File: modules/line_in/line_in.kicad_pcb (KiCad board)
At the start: 2 copper layers, 27.9 x 66 mm, 2 parts

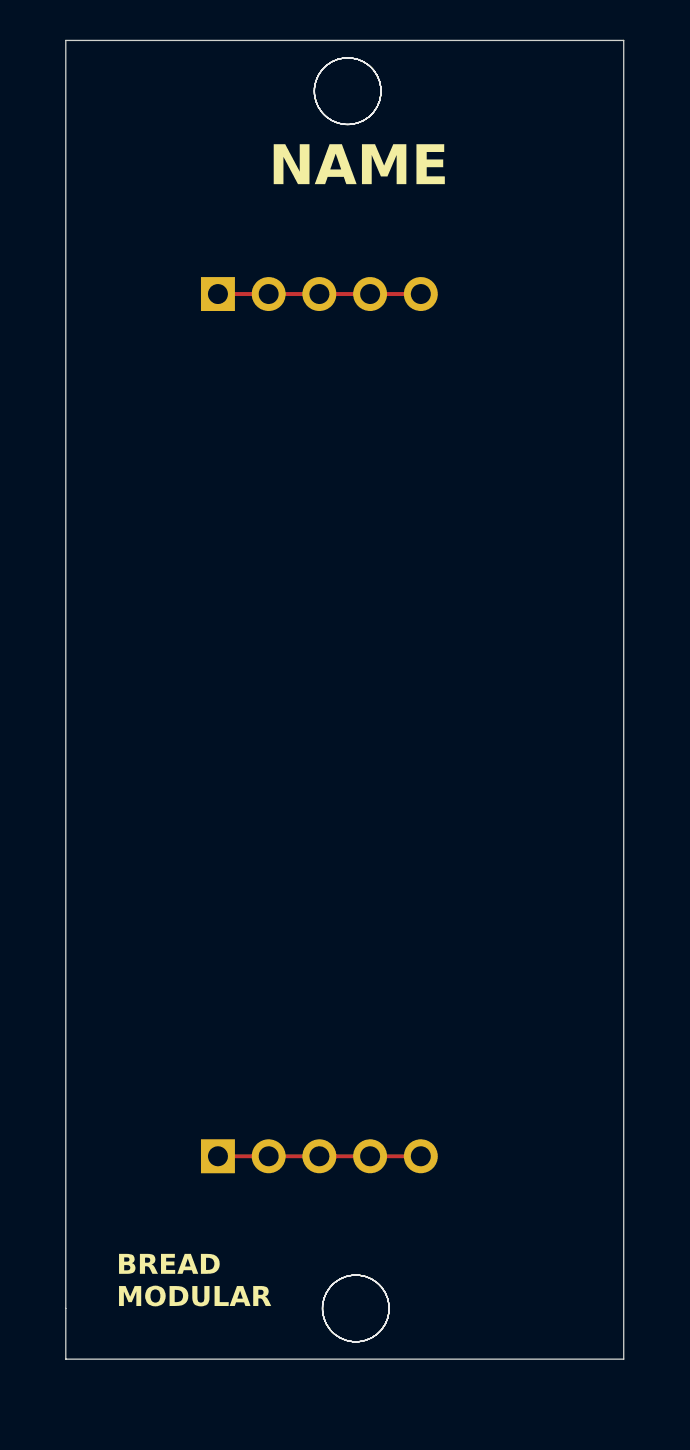
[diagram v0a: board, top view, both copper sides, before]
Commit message: Add the schematic for the PCB
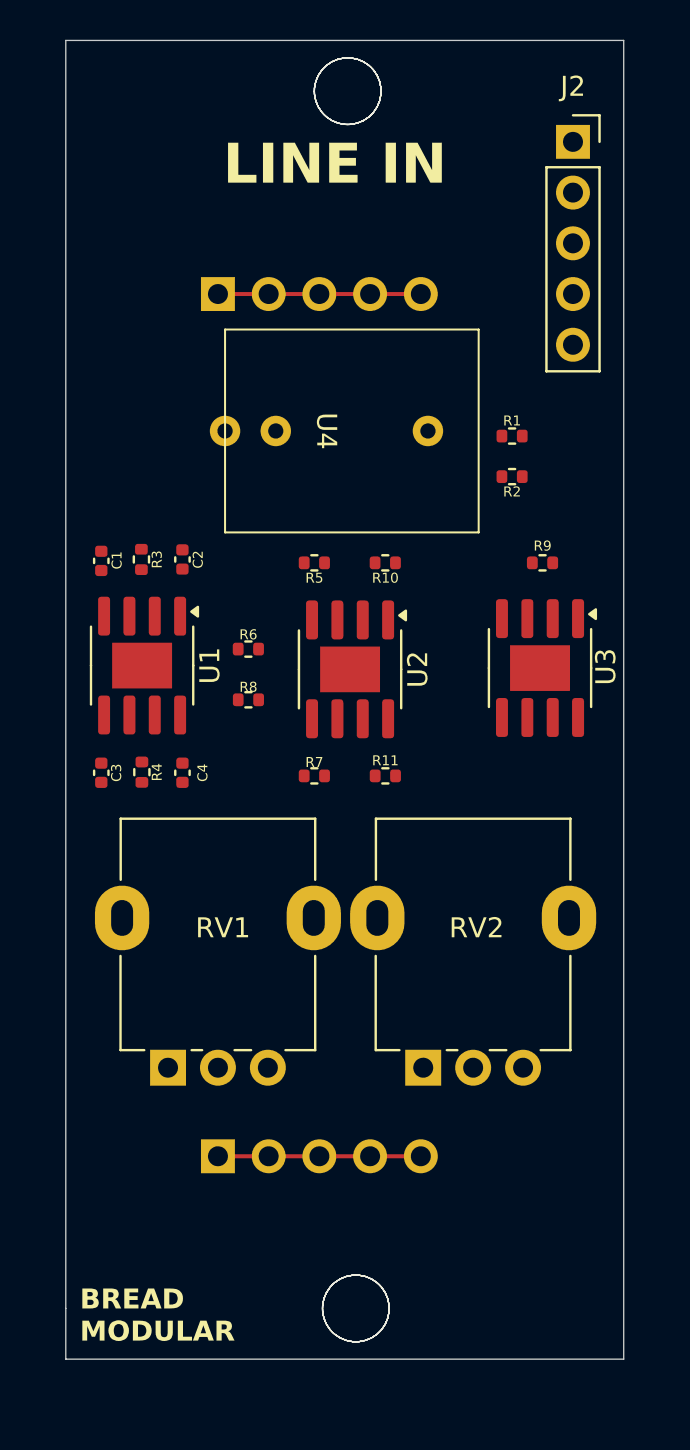
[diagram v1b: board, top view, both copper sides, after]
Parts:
- added C1: 0.1uf, Capacitor_SMD:C_0402_1005Metric, F.Cu at (50.0, 66.7)
- added C2: 33pf, Capacitor_SMD:C_0402_1005Metric, F.Cu at (54.1, 66.6)
- added C3: 0.1uf, Capacitor_SMD:C_0402_1005Metric, F.Cu at (50.0, 77.3)
- added C4: 33pf, Capacitor_SMD:C_0402_1005Metric, F.Cu at (54.1, 77.3)
- added J2: Outputs, Connector_PinSocket_2.54mm:PinSocket_1x05_P2.54mm_Vertical, F.Cu at (73.7, 45.7)
- added R1: 1K, Resistor_SMD:R_0402_1005Metric, F.Cu at (70.6, 60.5)
- added R10: 100K, Resistor_SMD:R_0402_1005Metric, F.Cu at (64.3, 66.8)
- added R11: 100K, Resistor_SMD:R_0402_1005Metric, F.Cu at (64.3, 77.5)
- added R2: 1K, Resistor_SMD:R_0402_1005Metric, F.Cu at (70.6, 62.5)
- added R3: 100K, Resistor_SMD:R_0402_1005Metric, F.Cu at (52.0, 66.6)
- added R4: 100K, Resistor_SMD:R_0402_1005Metric, F.Cu at (52.1, 77.3)
- added R5: 100K, Resistor_SMD:R_0402_1005Metric, F.Cu at (60.7, 66.8)
- added R6: 10K, Resistor_SMD:R_0402_1005Metric, F.Cu at (57.4, 71.1)
- added R7: 100K, Resistor_SMD:R_0402_1005Metric, F.Cu at (60.7, 77.5)
- added R8: 10K, Resistor_SMD:R_0402_1005Metric, F.Cu at (57.4, 73.7)
- added R9: 51K, Resistor_SMD:R_0402_1005Metric, F.Cu at (72.1, 66.8)
- added RV1: 100K, Potentiometer_THT:Potentiometer_Alpha_RD901F-40-00D_Single_Vertical, F.Cu at (53.4, 92.1)
- added RV2: 100K, Potentiometer_THT:Potentiometer_Alpha_RD901F-40-00D_Single_Vertical, F.Cu at (66.2, 92.1)
- added U1: LM358, Package_SO:SOIC-8-1EP_3.9x4.9mm_P1.27mm_EP2.29x3mm, F.Cu at (52.1, 71.9)
- added U2: LM358, Package_SO:SOIC-8-1EP_3.9x4.9mm_P1.27mm_EP2.29x3mm, F.Cu at (62.5, 72.1)
- added U3: LM358, Package_SO:SOIC-8-1EP_3.9x4.9mm_P1.27mm_EP2.29x3mm, F.Cu at (72.0, 72.1)
- added U4: ~, Footprints:Audio_Socket_TRS_3.5mm, F.Cu at (61.3, 60.2)
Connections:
- 5V1 pad 1: unconnected-(5V1-Pin_1-Pad1) -> +5V
- 5V1 pad 2: unconnected-(5V1-Pin_2-Pad2) -> +5V
- 5V1 pad 3: unconnected-(5V1-Pin_3-Pad3) -> +5V
- 5V1 pad 4: unconnected-(5V1-Pin_4-Pad4) -> +5V
- 5V1 pad 5: unconnected-(5V1-Pin_5-Pad5) -> +5V
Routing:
- net Net-(U1A-+): track 0.00 -> 0.71 mm
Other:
- board text added: "LINE IN"
- board text removed: "NAME"

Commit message: Update the line-in module
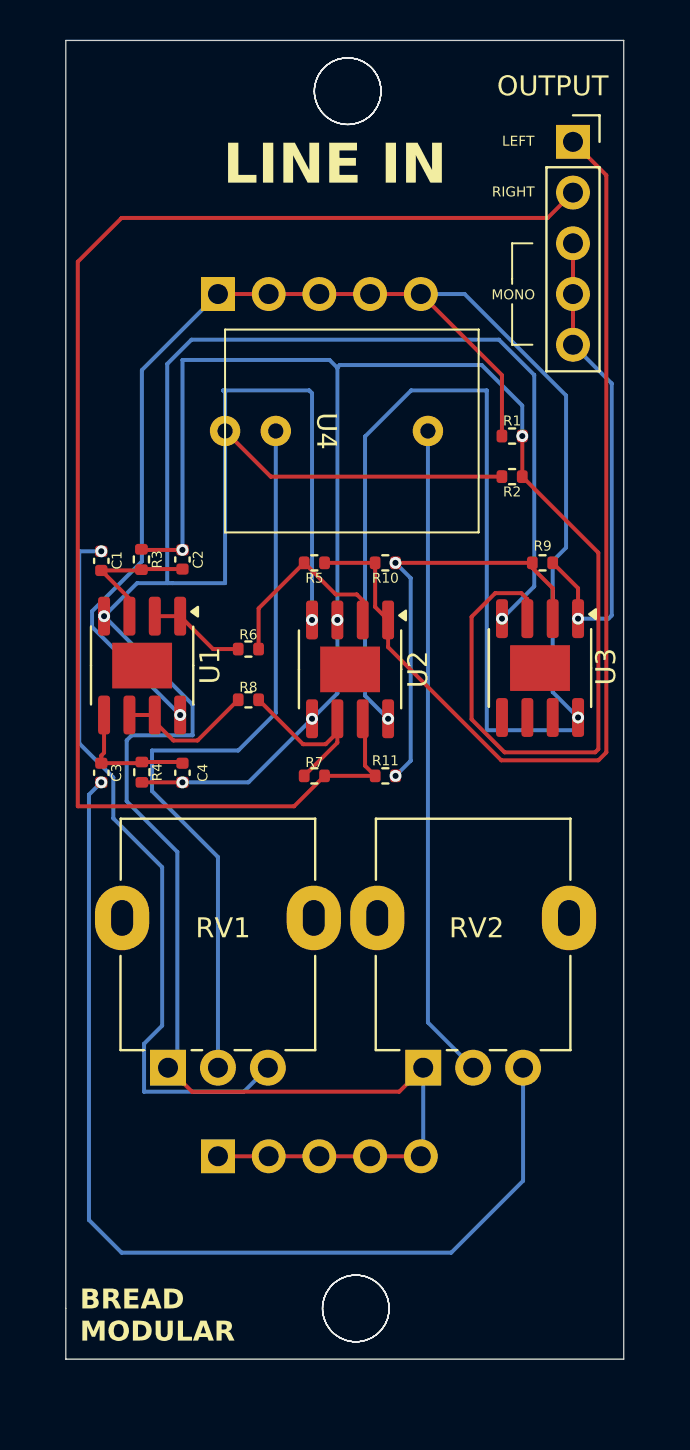
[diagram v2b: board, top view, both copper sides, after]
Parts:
- renumbered J2 to OUTPUT
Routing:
- net GND: track 10.2 -> 147.9 mm, vias 0 -> 3
- net +5V: track 0.00 -> 104.5 mm, vias 0 -> 3
- net Net-(U2A-+): track 0.00 -> 93.0 mm, vias 0 -> 5
- net OUT_R: track 0.00 -> 72.1 mm
- net IN R: track 0.00 -> 51.7 mm, vias 0 -> 1
- net OUT_L: track 0.00 -> 51.7 mm
- net Net-(U4-TIP): track 0.00 -> 38.4 mm
- net IN L: track 0.00 -> 37.0 mm, vias 0 -> 1
- net Net-(U4-RING): track 0.00 -> 32.8 mm
- net OUT_MONO: track 0.00 -> 24.5 mm, vias 0 -> 1
- net Net-(U3A--): track 0.00 -> 21.4 mm, vias 0 -> 2
- net Net-(U2A--): track 0.00 -> 9.95 mm
- net Net-(U2B--): track 0.00 -> 9.35 mm
- net Net-(U1B--): track 0.00 -> 7.02 mm
- net Net-(U1B-+): track 0.00 -> 6.58 mm
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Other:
- board text added: "LEFT"
- board text added: "MONO"
- board text added: "RIGHT"

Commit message: Make sure SMD via are not placed on pads.
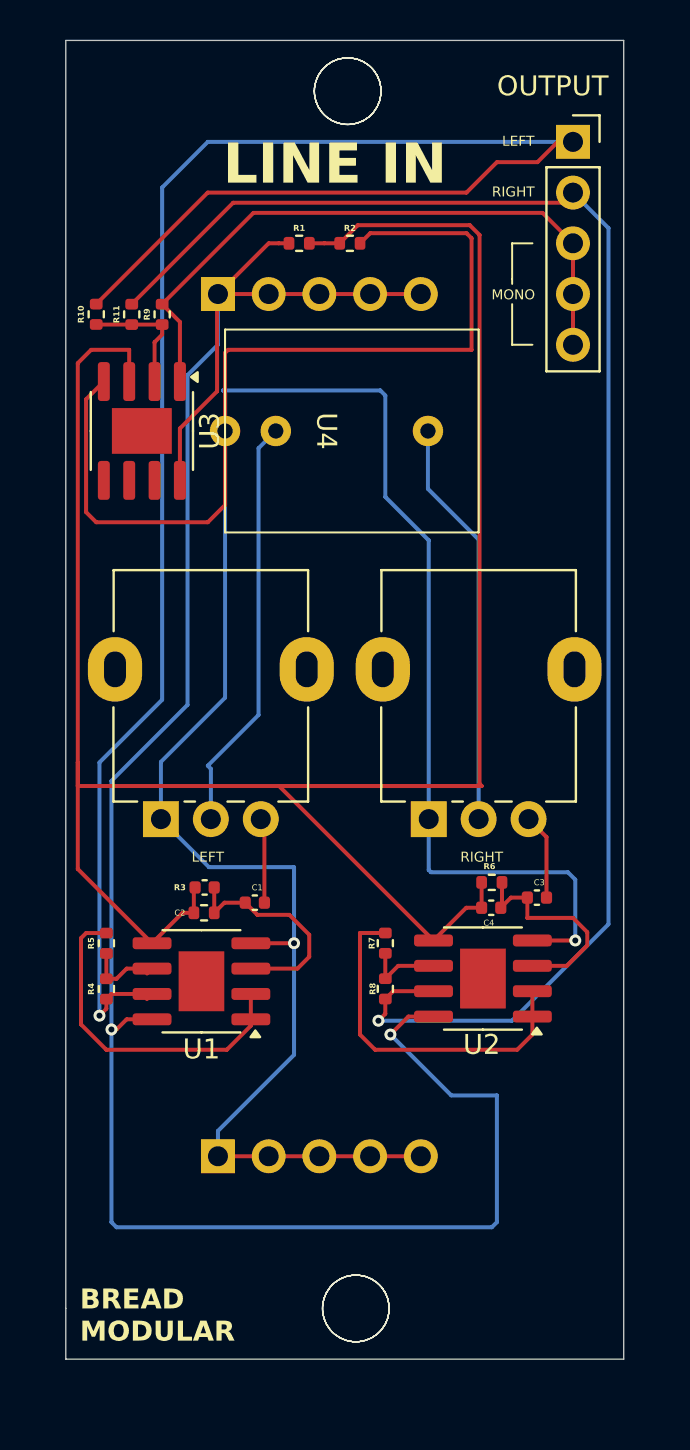
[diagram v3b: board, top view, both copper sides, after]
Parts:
- removed RV1, RV2: 100K, Potentiometer_THT:Potentiometer_Alpha_RD901F-40-00D_Single_Vertical
- added LEFT: 100K, Potentiometer_THT:Potentiometer_Alpha_RD901F-40-00D_Single_Vertical, F.Cu at (53.0, 79.6)
- added RIGHT: 100K, Potentiometer_THT:Potentiometer_Alpha_RD901F-40-00D_Single_Vertical, F.Cu at (66.4, 79.6)
- R5, R7: value 100K -> 10K
- R6, R8: value 10K -> 100K
- moved R11 26.4 mm to (51.6, 54.4), turned to -90 degrees
- moved U3 23.2 mm to (52.1, 60.2)
- moved R9 22.8 mm to (53.1, 54.4), turned to 90 degrees
- moved C3 22.7 mm to (71.9, 83.6), turned to 0 degrees
- moved R5 21.7 mm to (50.3, 85.9), turned to 90 degrees
- moved R10 19.1 mm to (49.8, 54.4), turned to -90 degrees
- moved C1 18.8 mm to (57.7, 83.8), turned to 0 degrees
- moved R3 18.0 mm to (55.2, 84.3), turned to 180 degrees
- moved R6 16.9 mm to (69.6, 82.8), turned to 180 degrees
- moved C4 16.9 mm to (69.6, 84.1), turned to 180 degrees
- moved U2 16.9 mm to (69.2, 87.6), turned to 180 degrees
- moved C2 16.5 mm to (55.2, 83.1), turned to 180 degrees
- moved U1 16.1 mm to (55.1, 87.8), turned to 180 degrees
- moved R8 16.0 mm to (64.3, 88.1), turned to 90 degrees
- moved R1 14.4 mm to (59.9, 50.8)
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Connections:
- C2 pad 2: Net-(U2A-+) -> 2.5V
- C3 pad 1: Net-(U1B-+) -> Net-(U2A-+)
- C4 pad 2: Net-(U1B-+) -> 2.5V
- R1 pad 2: Net-(U2A-+) -> 2.5V
- R2 pad 1: Net-(U2A-+) -> 2.5V
- R3 pad 2: Net-(U2A-+) -> 2.5V
- R4 pad 1: Net-(U2A-+) -> OUT_L
- R4 pad 2: Net-(U1B-+) -> Net-(U1B--)
- R5 pad 1: Net-(U2A--) -> Net-(U1B--)
- R5 pad 2: OUT_L -> Net-(U1A--)
- R6 pad 1: Net-(U1A--) -> Net-(U2A-+)
- R6 pad 2: Net-(U2A--) -> 2.5V
- R7 pad 2: OUT_R -> Net-(U2A--)
- R8 pad 1: Net-(U1B--) -> OUT_R
- U1 pad 5: Net-(U1B-+) -> 2.5V
- U1 pad 7: Net-(U1B--) -> OUT_L
- U2 pad 1: OUT_L -> Net-(U2A--)
- U2 pad 5: Net-(U2A-+) -> 2.5V
- U3 pad 3: Net-(U2A-+) -> 2.5V
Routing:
- net 2.5V: track 0.00 -> 112.5 mm
- net Net-(U2A-+): track 93.0 -> 11.0 mm, vias 5 -> 0
- net IN R: track 51.7 -> 4.30 mm, vias 1 -> 0
- net OUT_L: track 51.7 -> 95.3 mm, vias 0 -> 1
- net IN L: track 37.0 -> 4.26 mm, vias 1 -> 0
- net Net-(U4-TIP): track 38.4 -> 20.9 mm
- net Net-(U3A--): track 21.4 -> 6.32 mm, vias 2 -> 0
- net Net-(U4-RING): track 32.8 -> 20.5 mm
- net Net-(U1A--): track 4.86 -> 16.8 mm
- net OUT_MONO: track 24.5 -> 32.4 mm, vias 1 -> 0
- net Net-(U2A--): track 9.95 -> 17.8 mm
- net OUT_R: track 72.1 -> 79.1 mm, vias 0 -> 1
- net Net-(U1B-+): track 6.58 -> 0.00 mm
- net +5V: track 104.5 -> 110.8 mm, vias 3 -> 2
- net Net-(U2B--): track 9.35 -> 3.95 mm
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
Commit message: version line_in_0.2.0
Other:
- board text added: "line_in_0.2.0"
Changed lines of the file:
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@@
+		)
+	)
+	(gr_text "line_in_0.2.0"
+		(at 70.612 105.918 0)
+		(layer "F.SilkS")
+		(effects
+			(font
+				(size 0.5 0.5)
+				(thickness 0.075)
+			)
+			(justify left bottom)
 		)
 	)

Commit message: Start working on the new version of line_in
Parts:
- removed C1, C3: 0.1uf, Capacitor_SMD:C_0402_1005Metric
- removed C2, C4: 33pf, Capacitor_SMD:C_0402_1005Metric
- removed LEFT, RIGHT: 100K, Potentiometer_THT:Potentiometer_Alpha_RD901F-40-00D_Single_Vertical
- removed OUTPUT: Outputs, Connector_PinSocket_2.54mm:PinSocket_1x05_P2.54mm_Vertical
- removed R1, R2: 1K, Resistor_SMD:R_0402_1005Metric
- removed R10, R11, R3, R4, R6, R8: 100K, Resistor_SMD:R_0402_1005Metric
- removed R5, R7: 10K, Resistor_SMD:R_0402_1005Metric
- removed R9: 51K, Resistor_SMD:R_0402_1005Metric
- removed U1, U2, U3: LM358, Package_SO:SOIC-8-1EP_3.9x4.9mm_P1.27mm_EP2.29x3mm
- removed U4: ~, Footprints:Audio_Socket_TRS_3.5mm
- added INPUT1: Conn_01x05_Socket, Connector_PinSocket_2.54mm:PinSocket_1x05_P2.54mm_Vertical, F.Cu at (50.8, 45.7)
- added OUTPUT2: Conn_01x05_Socket, Connector_PinSocket_2.54mm:PinSocket_1x05_P2.54mm_Vertical, F.Cu at (73.7, 45.7)
- moved 5V1 2.54 mm to (55.9, 50.8)
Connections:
- net +5V renamed Net-(5V1-Pin_1)
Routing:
- net GND: track 150.5 -> 10.2 mm, vias 2 -> 0
- net 2.5V: track 112.5 -> 0.00 mm
- net Net-(5V1-Pin_1): track 110.8 -> 10.2 mm, vias 2 -> 0
- net OUT_L: track 95.3 -> 0.00 mm, vias 1 -> 0
- net OUT_R: track 79.1 -> 0.00 mm, vias 1 -> 0
- net OUT_MONO: track 32.4 -> 0.00 mm
- net Net-(U4-TIP): track 20.9 -> 0.00 mm
- net Net-(U4-RING): track 20.5 -> 0.00 mm
- net Net-(U2A--): track 17.8 -> 0.00 mm
- net Net-(U1A--): track 16.8 -> 0.00 mm
- net Net-(U1A-+): track 11.2 -> 0.00 mm
- net Net-(U2A-+): track 11.0 -> 0.00 mm
- net Net-(U3A--): track 6.32 -> 0.00 mm
- net IN R: track 4.30 -> 0.00 mm
- net IN L: track 4.26 -> 0.00 mm
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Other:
- board size 27.9 x 66 mm -> 30.5 x 68.6 mm
- board text added: "NAME"
- board text removed: "LEFT"
- board text removed: "LINE IN"
- board text removed: "MONO"
- board text removed: "RIGHT"
- board text removed: "line_in_0.2.0"
